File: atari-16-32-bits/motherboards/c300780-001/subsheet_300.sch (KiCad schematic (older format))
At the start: 4 parts, among them U300_DIP40 ST_DMA_DIP40_PHY, U300_PLCC44 ST_DMA_PLCC44_PHY

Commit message: Fixes #51 : [bug][schematics] fix the association of mlcc capacitors and their footprint in schematics to match the association done in the pcb
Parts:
- C302: footprint commons_passives_THT:Passive_THT_capacitor_ceramic_radial_W5.08mm_L6.35mm_X11.43mm -> commons_passives_THT:Passive_THT_capacitor_mlcc_W2.54mm_L7.62mm
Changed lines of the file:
@@
 F 0 "C302" H 3025 4600 50  0000 L CNN
 F 1 "0.1uF" H 3025 4400 50  0000 L CNN
-F 2 "commons_passives_THT:Passive_THT_capacitor_ceramic_radial_W5.08mm_L6.35mm_X11.43mm" H 3038 4350 50  0001 C CNN
+F 2 "commons_passives_THT:Passive_THT_capacitor_mlcc_W2.54mm_L7.62mm" H 3038 4350 50  0001 C CNN
 F 3 "~" H 3000 4500 50  0001 C CNN
 	1    3000 4500

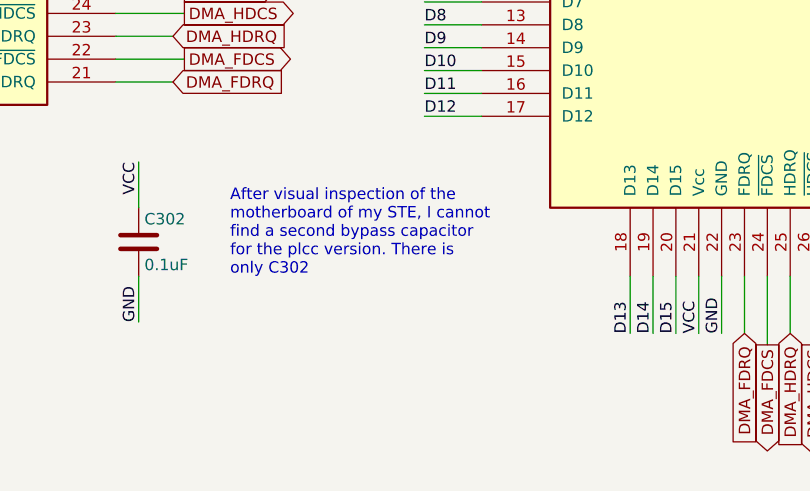
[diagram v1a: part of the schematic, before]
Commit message: Fixed schematics : missing C226 found on real motherboard
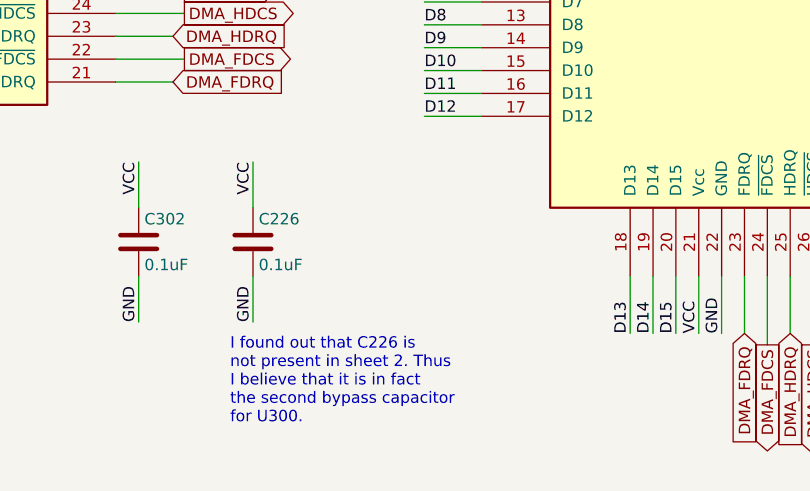
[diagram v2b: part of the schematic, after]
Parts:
- added C226: 0.1uF, commons_passives_THT:Passive_THT_capacitor_mlcc_W2.54mm_L7.62mm, symbol Device:C
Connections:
- net GND: now also C226.2
- net VCC: now also C226.1
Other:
- note added: "I found out that C226 is\nnot present in sheet 2. Thus\nI believe that it is in fact\nthe second bypass capacitor \nfor U300."
- note removed: "After visual inspection of the\nmotherboard of my STE, I cannot\nfind a second bypass capacitor\nfor the plcc version. There is \nonly C302"
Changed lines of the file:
@@
 Wire Wire Line
 	3000 4650 3000 4850
-Text Notes 3400 4650 0    50   ~ 0
-After visual inspection of the\nmotherboard of my STE, I cannot\nfind a second bypass capacitor\nfor the plcc version. There is \nonly C302
+Text Notes 3400 5300 0    50   ~ 0
+I found out that C226 is\nnot present in sheet 2. Thus\nI believe that it is in fact\nthe second bypass capacitor \nfor U300.
 Wire Wire Line
 	4350 2000 4500 2000
@@
 Wire Wire Line
 	5650 4650 5650 4900
+$Comp
+L Device:C C?
+U 1 1 60FC622A
+P 3500 4500
+AR Path="/60786F27/6078774E/60FC622A" Ref="C?"  Part="1"
+AR Path="/60786F27/607875AF/60FC622A" Ref="C?"  Part="1"
+AR Path="/6089D0BA/60FC622A" Ref="C?"  Part="1"
+AR Path="/608A2359/60FC622A" Ref="C?"  Part="1"
+AR Path="/60A1445F/60FC622A" Ref="C226"  Part="1"
+F 0 "C226" H 3525 4600 50  0000 L CNN
+F 1 "0.1uF" H 3525 4400 50  0000 L CNN
+F 2 "commons_passives_THT:Passive_THT_capacitor_mlcc_W2.54mm_L7.62mm" H 3538 4350 50  0001 C CNN
+F 3 "~" H 3500 4500 50  0001 C CNN
+	1    3500 4500
+	1    0    0    -1
+$EndComp
+Text Label 3500 4850 1    50   ~ 0
+GND
+Text Label 3500 4150 3    50   ~ 0
+VCC
+Wire Wire Line
+	3500 4150 3500 4350
+Wire Wire Line
+	3500 4650 3500 4850
 $EndSCHEMATC
